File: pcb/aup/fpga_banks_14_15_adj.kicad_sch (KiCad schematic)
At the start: 1 part, among them U1 XC7A50T-2FGG484C

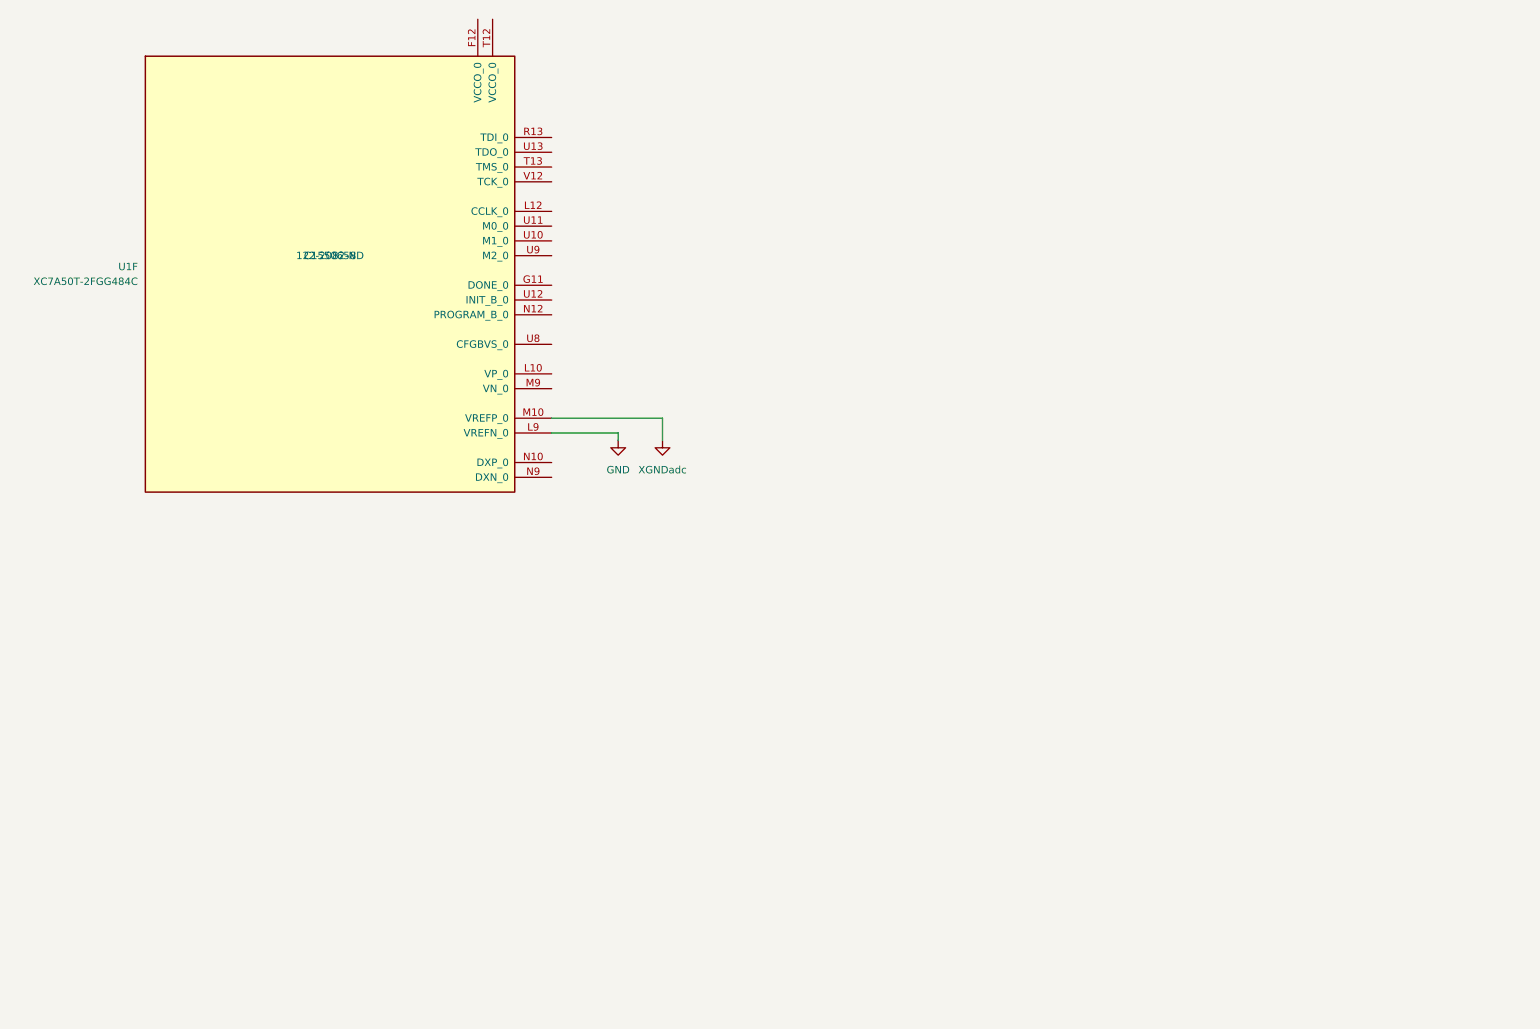
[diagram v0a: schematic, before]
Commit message: Add hierarchical sheets for banks and add caps.
There are some stale sheets in this commit, but I don't want to delete
an active one accidentally. Save them all for now, and then go back and
clean them up.
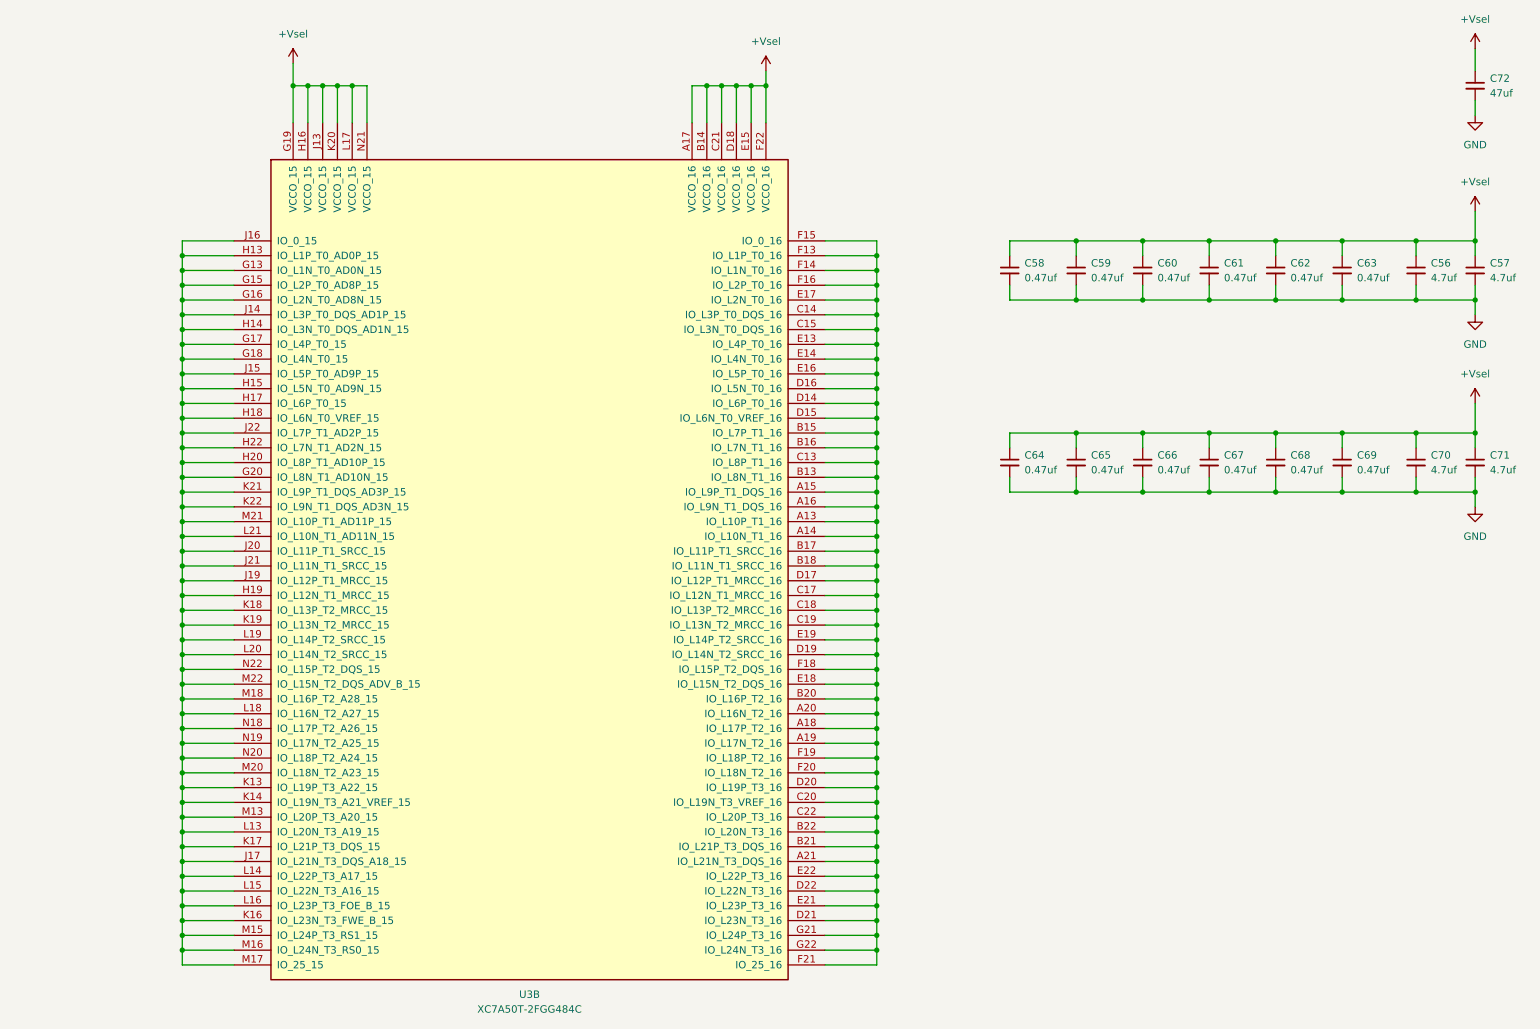
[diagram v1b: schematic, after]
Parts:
- removed U1: XC7A50T-2FGG484C, !Xilinx:Xilinx_FGG484, symbol !Xilinx:XC7A50T-FGG484
- added C56, C57, C70, C71: 4.7uf, Capacitor_SMD:C_0805_2012Metric, symbol !Misc:C_4.7uf_0805
- added C58, C59, C60, C61, C62, C63, C64, C65, C66, C67, C68, C69: 0.47uf, Capacitor_SMD:C_0402_1005Metric, symbol !Misc:C_0.47uf_0402
- added C72: 47uf, Capacitor_SMD:C_1206_3216Metric, symbol !Misc:C_47uf_1206
- added U3: XC7A50T-2FGG484C, !Xilinx:Xilinx_FGG484, symbol !Xilinx:XC7A50T-FGG484
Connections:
- net GND: now also C56.2, C57.2, C58.2, C59.2, C60.2, C61.2, C62.2, C63.2, C64.2, C65.2, C66.2, C67.2, C68.2, C69.2, C70.2, C71.2, C72.2
- new net: U3.A13 (IO_L10P_T1_16), U3.A14 (IO_L10N_T1_16), U3.A15 (IO_L9P_T1_DQS_16), U3.A16 (IO_L9N_T1_DQS_16), U3.A18 (IO_L17P_T2_16), U3.A19 (IO_L17N_T2_16), U3.A20 (IO_L16N_T2_16), U3.A21 (IO_L21N_T3_DQS_16), U3.B13 (IO_L8N_T1_16), U3.B15 (IO_L7P_T1_16), U3.B16 (IO_L7N_T1_16), U3.B17 (IO_L11P_T1_SRCC_16), U3.B18 (IO_L11N_T1_SRCC_16), U3.B20 (IO_L16P_T2_16), U3.B21 (IO_L21P_T3_DQS_16), U3.B22 (IO_L20N_T3_16), U3.C13 (IO_L8P_T1_16), U3.C14 (IO_L3P_T0_DQS_16), U3.C15 (IO_L3N_T0_DQS_16), U3.C17 (IO_L12N_T1_MRCC_16), U3.C18 (IO_L13P_T2_MRCC_16), U3.C19 (IO_L13N_T2_MRCC_16), U3.C20 (IO_L19N_T3_VREF_16), U3.C22 (IO_L20P_T3_16), U3.D14 (IO_L6P_T0_16), U3.D15 (IO_L6N_T0_VREF_16), U3.D16 (IO_L5N_T0_16), U3.D17 (IO_L12P_T1_MRCC_16), U3.D19 (IO_L14N_T2_SRCC_16), U3.D20 (IO_L19P_T3_16), U3.D21 (IO_L23N_T3_16), U3.D22 (IO_L22N_T3_16), U3.E13 (IO_L4P_T0_16), U3.E14 (IO_L4N_T0_16), U3.E16 (IO_L5P_T0_16), U3.E17 (IO_L2N_T0_16), U3.E18 (IO_L15N_T2_DQS_16), U3.E19 (IO_L14P_T2_SRCC_16), U3.E21 (IO_L23P_T3_16), U3.E22 (IO_L22P_T3_16), U3.F13 (IO_L1P_T0_16), U3.F14 (IO_L1N_T0_16), U3.F15 (IO_0_16), U3.F16 (IO_L2P_T0_16), U3.F18 (IO_L15P_T2_DQS_16), U3.F19 (IO_L18P_T2_16), U3.F20 (IO_L18N_T2_16), U3.F21 (IO_25_16), U3.G21 (IO_L24P_T3_16), U3.G22 (IO_L24N_T3_16)
- new net: U3.G13 (IO_L1N_T0_AD0N_15), U3.G15 (IO_L2P_T0_AD8P_15), U3.G16 (IO_L2N_T0_AD8N_15), U3.G17 (IO_L4P_T0_15), U3.G18 (IO_L4N_T0_15), U3.G20 (IO_L8N_T1_AD10N_15), U3.H13 (IO_L1P_T0_AD0P_15), U3.H14 (IO_L3N_T0_DQS_AD1N_15), U3.H15 (IO_L5N_T0_AD9N_15), U3.H17 (IO_L6P_T0_15), U3.H18 (IO_L6N_T0_VREF_15), U3.H19 (IO_L12N_T1_MRCC_15), U3.H20 (IO_L8P_T1_AD10P_15), U3.H22 (IO_L7N_T1_AD2N_15), U3.J14 (IO_L3P_T0_DQS_AD1P_15), U3.J15 (IO_L5P_T0_AD9P_15), U3.J16 (IO_0_15), U3.J17 (IO_L21N_T3_DQS_A18_15), U3.J19 (IO_L12P_T1_MRCC_15), U3.J20 (IO_L11P_T1_SRCC_15), U3.J21 (IO_L11N_T1_SRCC_15), U3.J22 (IO_L7P_T1_AD2P_15), U3.K13 (IO_L19P_T3_A22_15), U3.K14 (IO_L19N_T3_A21_VREF_15), U3.K16 (IO_L23N_T3_FWE_B_15), U3.K17 (IO_L21P_T3_DQS_15), U3.K18 (IO_L13P_T2_MRCC_15), U3.K19 (IO_L13N_T2_MRCC_15), U3.K21 (IO_L9P_T1_DQS_AD3P_15), U3.K22 (IO_L9N_T1_DQS_AD3N_15), U3.L13 (IO_L20N_T3_A19_15), U3.L14 (IO_L22P_T3_A17_15), U3.L15 (IO_L22N_T3_A16_15), U3.L16 (IO_L23P_T3_FOE_B_15), U3.L18 (IO_L16N_T2_A27_15), U3.L19 (IO_L14P_T2_SRCC_15), U3.L20 (IO_L14N_T2_SRCC_15), U3.L21 (IO_L10N_T1_AD11N_15), U3.M13 (IO_L20P_T3_A20_15), U3.M15 (IO_L24P_T3_RS1_15), U3.M16 (IO_L24N_T3_RS0_15), U3.M17 (IO_25_15), U3.M18 (IO_L16P_T2_A28_15), U3.M20 (IO_L18N_T2_A23_15), U3.M21 (IO_L10P_T1_AD11P_15), U3.M22 (IO_L15N_T2_DQS_ADV_B_15), U3.N18 (IO_L17P_T2_A26_15), U3.N19 (IO_L17N_T2_A25_15), U3.N20 (IO_L18P_T2_A24_15), U3.N22 (IO_L15P_T2_DQS_15)
- new net +Vsel: C56.1, C57.1, C58.1, C59.1, C60.1, C61.1, C62.1, C63.1, C64.1, C65.1, C66.1, C67.1, C68.1, C69.1, C70.1, C71.1, C72.1, U3.A17 (VCCO_16), U3.B14 (VCCO_16), U3.C21 (VCCO_16), U3.D18 (VCCO_16), U3.E15 (VCCO_16), U3.F22 (VCCO_16), U3.G19 (VCCO_15), U3.H16 (VCCO_15), U3.J13 (VCCO_15), U3.K20 (VCCO_15), U3.L17 (VCCO_15), U3.N21 (VCCO_15)
